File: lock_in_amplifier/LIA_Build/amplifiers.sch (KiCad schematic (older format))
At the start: 16 parts, among them U10 OP1177, U9 OP1177

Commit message: power supply, amp chain first pass
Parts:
- removed C25: 0.1u, symbol C
- removed U10: OP1177, Housings_SSOP:MSOP-8-1EP_3x3mm_Pitch0.65mm, symbol OP1177
- added C30: 0.1u, Capacitors_SMD:C_0805, symbol C
- added J25: GAIN SEL - MID, symbol Conn_01x03
- added J28: ORDER OF MAGNITUDE SELECT, symbol Conn_01x05
- added J29: DECIMAL MULTIPLIER SELECT, symbol Conn_01x04
- added R16, R37, R40: 100k, Resistors_SMD:R_0805, symbol R
- added R17, R38, R39, R41: 10k, Resistors_SMD:R_0805, symbol R
- added R18, R42: 1k, Resistors_SMD:R_0805, symbol R
- added R19, R20: 1M, Resistors_SMD:R_0805, symbol R
- added U1: LM358, symbol LM358
- added U12: NC7SB3157, symbol NC7SB3157
- C23, C24, C26: footprint (none) -> Capacitors_SMD:C_0805
- R22, R23, R24, R26, R27, R28, R29, R30, R31: footprint (none) -> Resistors_SMD:R_0805
- R25: value 10k -> 100k; footprint (none) -> Resistors_SMD:R_0805
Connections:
- wire segments 40 -> 86
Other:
- note added: "1x2x5x select\n5x\n2x\n1x"
- note added: "GAIN SELECTION BLOCK. COMP. CT. MIN. W/ PARALLEL AND SERRIES COMPONENTS.\nALL GAINS V/V\n1000X\n500X\n200X\n100X\n50X\n20X\n10X\n5X\n2X\n1X"
- note added: "SP3T"
- note added: "SP4T"
- note added: "SPDT SWITCH\n"
- note added: "lower resistance values - higher current less resistor noise?"
- note added: "order of magnitude selector\n1000x\n100x\n10x\n1x"
- note added: "reason not to do this noise wise? issues with resistor noise?\nreplace last amp with lm358 or similar?"
- note removed: "dip switches\n"
- note removed: "reason not to do this noise wise? issues with resistor noise?"
- moved on the sheet: C23, C24, C26, R22, R23, R26, R27, R28, R29, R30, R31, U9

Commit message: initial transimpedance selection, lna refinement
amp overload led
switch comps added
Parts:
- removed J25: GAIN SEL - MID, symbol Conn_01x03
- removed J28: ORDER OF MAGNITUDE SELECT, symbol Conn_01x05
- removed J29: DECIMAL MULTIPLIER SELECT, symbol Conn_01x04
- removed U12: NC7SB3157, symbol NC7SB3157
- added C22: 0.1u, Capacitors_SMD:C_0805, symbol C
- added R53: 100k, symbol R
- added R54: 100, symbol R
- added S2: MID AMP GAIN SEL, symbol SPDT
- added S3: REF V SEL, symbol SPDT
- added S7: MAG SEL, symbol SP4T
- added S8: DECIMAL MULT SEL, symbol SP3T
- U1: footprint (none) -> SMD_Packages:SOIC-8-N
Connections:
- wire segments 86 -> 93
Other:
- note added: "reason not to do this noise wise? issues with resistor noise?"
- note removed: "SP3T"
- note removed: "SP4T"
- note removed: "reason not to do this noise wise? issues with resistor noise?\nreplace last amp with lm358 or similar?"
- moved on the sheet: C23, C24, C26, C30, R16, R17, R18, R19, R20, R22, R23, R24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

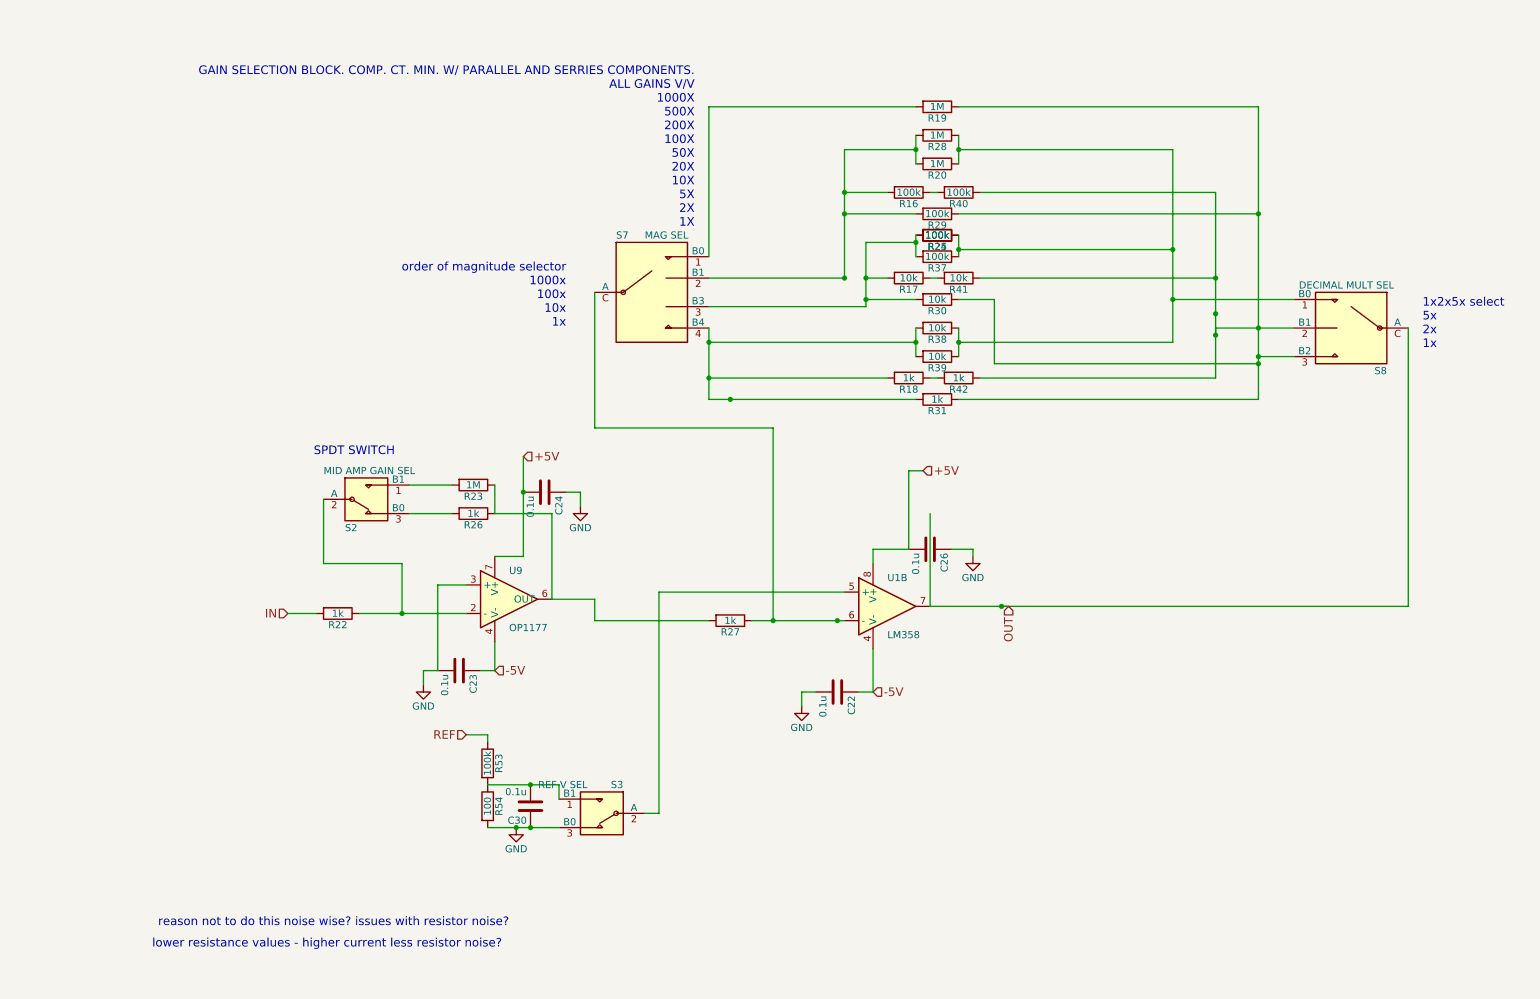
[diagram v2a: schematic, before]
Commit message: switch footprints, lm833 usage, pll investigation
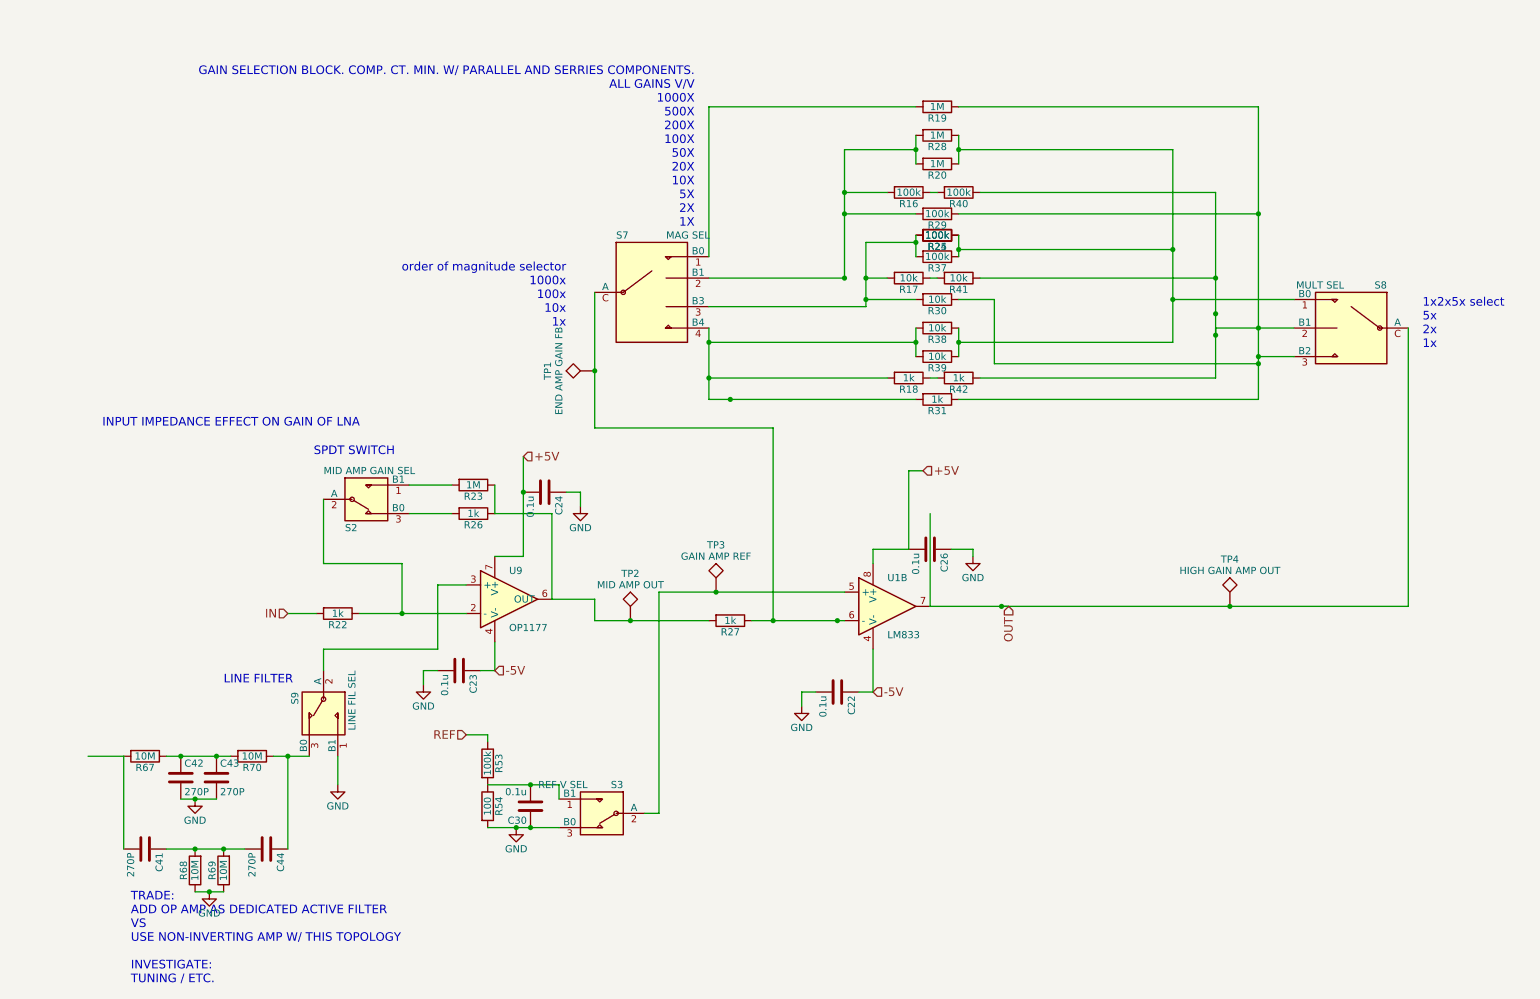
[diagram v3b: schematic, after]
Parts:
- added C41, C42, C43, C44: 270P, symbol C
- added R67, R68, R69, R70: 10M, symbol R
- added S9: LINE FIL SEL, footprints:SPDT_OS102011MS2QN1, symbol SPDT
- added TP1: END AMP GAIN FB, symbol TEST
- added TP2: MID AMP OUT, symbol TEST
- added TP3: GAIN AMP REF, symbol TEST
- added TP4: HIGH GAIN AMP OUT, symbol TEST
- S2, S3: footprint (none) -> footprints:SPDT_OS102011MS2QN1
- S7: footprint (none) -> footprints:SP4T_C&K_SS-14D0839-VG
- S8: value DECIMAL MULT SEL -> MULT SEL; footprint (none) -> footprints:SP3T_CK_SS-14D0839-VG
- U1: value LM358 -> LM833
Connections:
- net GND: now also C42.2, C43.2, R68.1, R69.1, S9.1 (B1); no longer U9.3 (+)
- net OUT: now also TP4.1
- net at S3.2 (A), U1.5 (+): now also TP3.1
- net at R27.1, S7.C (A), U1.6 (-): now also TP1.1
- net at R23.1, R26.1, R27.2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: now also TP2.1
- new net: S9.2 (A), U9.3 (+)
- new net: C44.1, R70.1, S9.3 (B0)
- new net: C42.1, C43.1, R67.1, R70.2
- new net: C41.2, R67.2
- new net: C41.1, C44.2, R68.2, R69.2
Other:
- note added: "INPUT IMPEDANCE EFFECT ON GAIN OF LNA"
- note added: "LINE FILTER"
- note added: "TRADE:\nADD OP AMP AS DEDICATED ACTIVE FILTER\nVS\nUSE NON-INVERTING AMP W/ THIS TOPOLOGY\n\nINVESTIGATE:\nTUNING / ETC."
- note removed: "lower resistance values - higher current less resistor noise?"
- note removed: "reason not to do this noise wise? issues with resistor noise?"

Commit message: PLL initial implementation
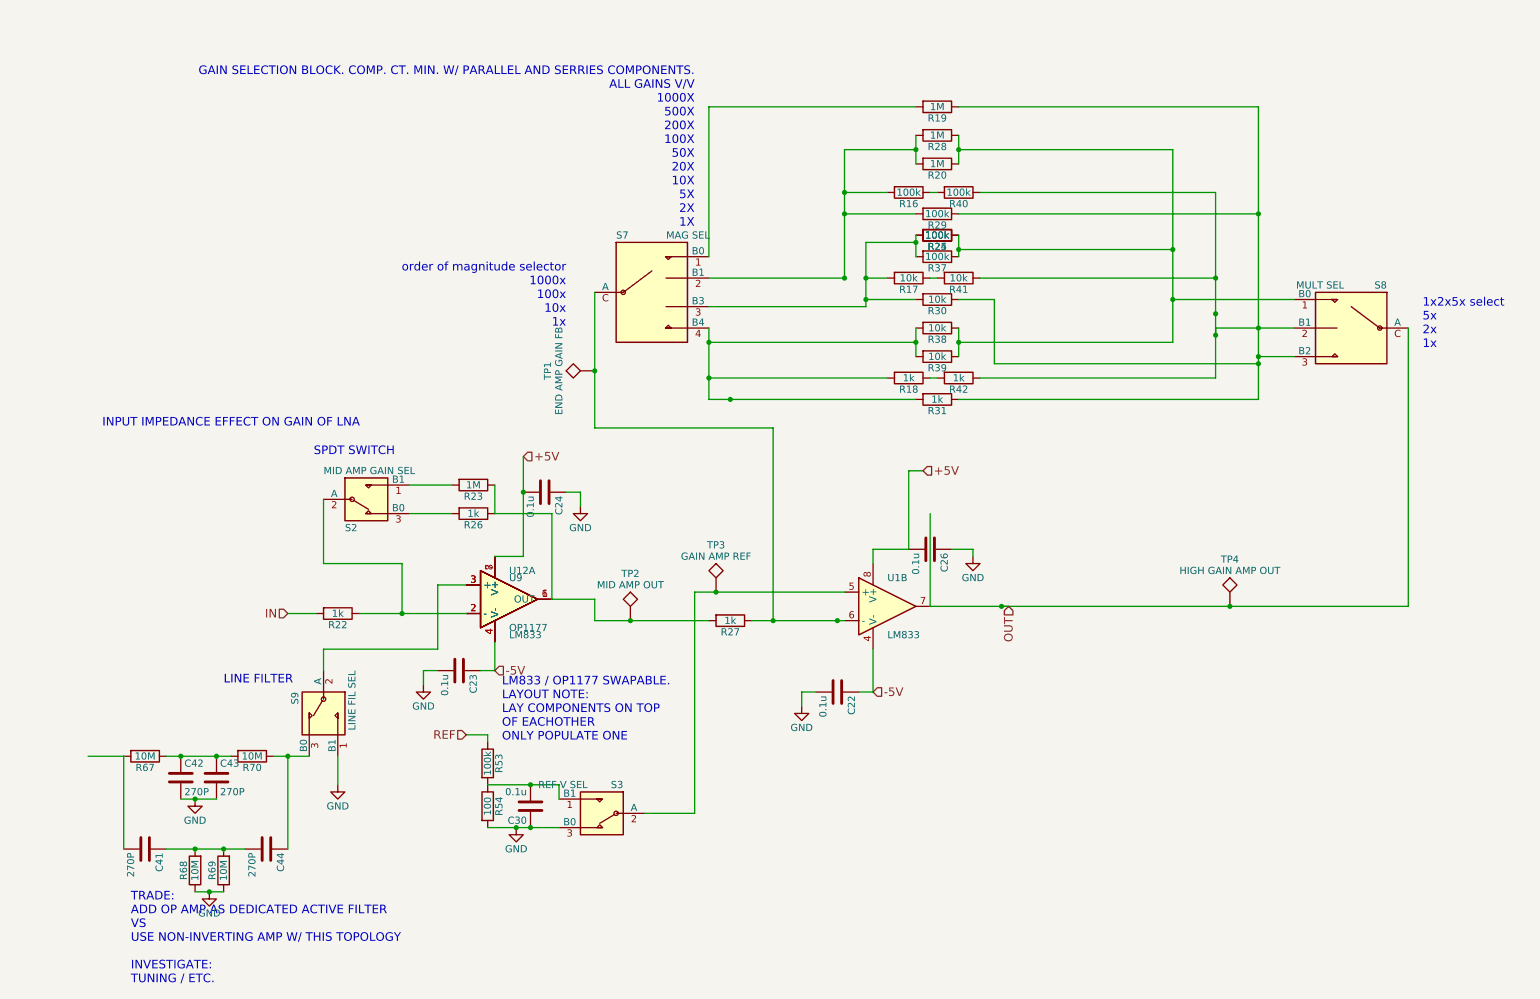
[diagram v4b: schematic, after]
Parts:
- added U12: LM833, symbol LM833
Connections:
- net +5V: now also U12.8 (V+)
- net -5V: now also U12.4 (V-)
- net at R22.1, S2.2 (A), U9.2 (-): now also U12.2 (-)
- net at R23.1, R26.1, R27.2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: now also U12.1
- net at S9.2 (A), U9.3 (+): now also U12.3 (+)
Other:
- note added: "LM833 / OP1177 SWAPABLE.\nLAYOUT NOTE: \nLAY COMPONENTS ON TOP \nOF EACHOTHER\nONLY POPULATE ONE"
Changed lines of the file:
@@
 $EndComp
 $Comp
-L GND #PWR055
+L GND #PWR60
 U 1 1 5A225760
 P 7050 4350
-F 0 "#PWR055" H 7050 4100 50  0001 C CNN
+F 0 "#PWR60" H 7050 4100 50  0001 C CNN
 F 1 "GND" H 7050 4200 50  0000 C CNN
 F 2 "" H 7050 4350 50  0001 C CNN
@@
 $EndComp
 $Comp
-L GND #PWR056
+L GND #PWR56
 U 1 1 5A2257E8
 P 3200 5250
-F 0 "#PWR056" H 3200 5000 50  0001 C CNN
+F 0 "#PWR56" H 3200 5000 50  0001 C CNN
 F 1 "GND" H 3200 5100 50  0000 C CNN
 F 2 "" H 3200 5250 50  0001 C CNN
@@
 $EndComp
 $Comp
-L GND #PWR057
+L GND #PWR58
 U 1 1 5A22582C
 P 4300 4000
-F 0 "#PWR057" H 4300 3750 50  0001 C CNN
+F 0 "#PWR58" H 4300 3750 50  0001 C CNN
 F 1 "GND" H 4300 3850 50  0000 C CNN
 F 2 "" H 4300 4000 50  0001 C CNN
@@
 U 1 1 5A22674B
 P 3800 4650
-F 0 "U9" H 3800 4850 50  0000 L CNN
+F 0 "U9" H 3800 4800 50  0000 L CNN
 F 1 "OP1177" H 3800 4450 50  0000 L CNN
 F 2 "Housings_SSOP:MSOP-8-1EP_3x3mm_Pitch0.65mm" H 4050 4350 50  0001 C CNN
@@
 $EndComp
 $Comp
-L GND #PWR058
+L GND #PWR57
 U 1 1 5A237D65
 P 3850 6250
-F 0 "#PWR058" H 3850 6000 50  0001 C CNN
+F 0 "#PWR57" H 3850 6000 50  0001 C CNN
 F 1 "GND" H 3850 6100 50  0000 C CNN
 F 2 "" H 3850 6250 50  0001 C CNN
@@
 	3900 4350 3700 4350
 Wire Wire Line
-	3900 3650 3900 4350
-Wire Wire Line
-	6750 4700 7300 4700
+	3900 3650 3900 3900
+Wire Wire Line
+	3900 3900 3900 4350
+Wire Wire Line
+	6750 4700 7250 4700
+Wire Wire Line
+	7250 4700 7300 4700
 Wire Wire Line
 	6750 4050 6750 4700
@@
 	3200 5150 3200 5250
 Wire Wire Line
-	5500 4800 6150 4800
+	5500 4800 5650 4800
+Wire Wire Line
+	5650 4800 6100 4800
+Wire Wire Line
+	6100 4800 6150 4800
 Connection ~ 6100 4800
 Wire Wire Line
@@
 	4100 4650 4400 4650
 Wire Wire Line
-	4750 6150 4850 6150
-Wire Wire Line
-	3650 6250 4150 6250
+	4750 6150 5100 6150
+Wire Wire Line
+	3650 6250 3850 6250
+Wire Wire Line
+	3850 6250 3950 6250
+Wire Wire Line
+	3950 6250 4150 6250
 Connection ~ 3950 6250
 Wire Wire Line
-	3650 5950 4150 5950
+	3650 5950 3950 5950
+Wire Wire Line
+	3950 5950 4150 5950
 Wire Wire Line
 	4150 5950 4150 6050
@@
 	4400 4650 4400 4800
 Wire Wire Line
-	4400 4800 5200 4800
-Wire Wire Line
-	4850 6150 4850 4600
-Wire Wire Line
-	4850 4600 6150 4600
+	4400 4800 4650 4800
+Wire Wire Line
+	4650 4800 5200 4800
+Wire Wire Line
+	5100 6150 5100 4600
+Wire Wire Line
+	5100 4600 5250 4600
+Wire Wire Line
+	5250 4600 6150 4600
 Wire Wire Line
 	3700 3850 3700 4050
@@
 	3400 4050 3100 4050
 Wire Wire Line
-	2750 4750 3500 4750
-Wire Wire Line
-	6950 2750 6950 2950
-Wire Wire Line
-	6950 2100 6950 2250
-Wire Wire Line
-	6950 1400 6950 1600
+	2750 4750 3050 4750
+Wire Wire Line
+	3050 4750 3500 4750
+Wire Wire Line
+	6950 2750 6950 2850
+Wire Wire Line
+	6950 2850 6950 2950
+Wire Wire Line
+	6950 2100 6950 2200
+Wire Wire Line
+	6950 2200 6950 2250
+Wire Wire Line
+	6950 1400 6950 1500
+Wire Wire Line
+	6950 1500 6950 1600
 Connection ~ 6950 1500
 Connection ~ 6950 2200
@@
 	6800 1800 6750 1800
 Wire Wire Line
-	6650 1400 6650 1600
-Wire Wire Line
-	6650 2100 6650 2250
-Wire Wire Line
-	6650 2750 6650 2950
+	6650 1400 6650 1500
+Wire Wire Line
+	6650 1500 6650 1600
+Wire Wire Line
+	6650 2100 6650 2150
+Wire Wire Line
+	6650 2150 6650 2250
+Wire Wire Line
+	6650 2750 6650 2850
+Wire Wire Line
+	6650 2850 6650 2950
 Connection ~ 6650 1500
 Connection ~ 6650 2850
@@
 Connection ~ 7250 4700
 Wire Wire Line
-	7250 4700 10100 4700
+	7250 4700 8850 4700
+Wire Wire Line
+	8850 4700 10100 4700
 Text Notes 10200 2900 0    60   ~ 0
 1x2x5x select\n5x\n2x\n1x
 Wire Wire Line
-	9050 1200 9050 3250
+	9050 1200 9050 1950
+Wire Wire Line
+	9050 1950 9050 2750
+Wire Wire Line
+	9050 2750 9050 2950
+Wire Wire Line
+	9050 2950 9050 3000
+Wire Wire Line
+	9050 3000 9050 3250
 Wire Wire Line
 	9050 3250 6950 3250
@@
 Connection ~ 9050 1950
 Wire Wire Line
-	8750 1800 8750 3100
+	8750 1800 8750 2400
+Wire Wire Line
+	8750 2400 8750 2650
+Wire Wire Line
+	8750 2650 8750 2800
+Wire Wire Line
+	8750 2800 8750 3100
 Wire Wire Line
 	8750 1800 7100 1800
@@
 Connection ~ 9050 3000
 Wire Wire Line
-	8450 1500 8450 2850
+	8450 1500 8450 2200
+Wire Wire Line
+	8450 2200 8450 2550
+Wire Wire Line
+	8450 2550 8450 2850
 Wire Wire Line
 	8450 2850 6950 2850
@@
 	5200 1200 6650 1200
 Wire Wire Line
-	5200 3250 6650 3250
+	5200 3250 5350 3250
+Wire Wire Line
+	5350 3250 6650 3250
 Wire Wire Line
 	6300 2550 6650 2550
@@
 	6450 2400 6300 2400
 Wire Wire Line
-	6300 2150 6300 2600
+	6300 2150 6300 2400
+Wire Wire Line
+	6300 2400 6300 2550
+Wire Wire Line
+	6300 2550 6300 2600
 Connection ~ 6300 2550
 Wire Wire Line
@@
 	6150 1950 6650 1950
 Wire Wire Line
-	6150 1500 6150 2400
+	6150 1500 6150 1800
+Wire Wire Line
+	6150 1800 6150 1950
+Wire Wire Line
+	6150 1950 6150 2400
 Wire Wire Line
 	6450 1800 6150 1800
@@
 $EndComp
 $Comp
-L GND #PWR059
+L GND #PWR59
 U 1 1 5A275732
 P 5850 5400
-F 0 "#PWR059" H 5850 5150 50  0001 C CNN
+F 0 "#PWR59" H 5850 5150 50  0001 C CNN
 F 1 "GND" H 5850 5250 50  0000 C CNN
 F 2 "" H 5850 5400 50  0001 C CNN
@@
 Connection ~ 9050 2950
 Wire Wire Line
-	8750 2750 9300 2750
+	8750 2750 9050 2750
+Wire Wire Line
+	9050 2750 9300 2750
 Wire Wire Line
 	8750 2750 8750 2800
@@
 	5200 1200 5200 2250
 Wire Wire Line
-	5200 2750 5200 3250
+	5200 2750 5200 2850
+Wire Wire Line
+	5200 2850 5200 3100
+Wire Wire Line
+	5200 3100 5200 3250
 Connection ~ 5350 3250
 Wire Wire Line
@@
 Connection ~ 6150 2400
 Wire Wire Line
-	4400 2500 4400 3450
+	4400 2500 4400 3050
+Wire Wire Line
+	4400 3050 4400 3450
 Wire Wire Line
 	4400 3450 5650 3450
@@
 	2500 5000 2500 5150
 $Comp
-L GND #PWR060
+L GND #PWR55
 U 1 1 5A257877
 P 2600 5950
-F 0 "#PWR060" H 2600 5700 50  0001 C CNN
+F 0 "#PWR55" H 2600 5700 50  0001 C CNN
 F 1 "GND" H 2600 5800 50  0000 C CNN
 F 2 "" H 2600 5950 50  0001 C CNN
@@
 $EndComp
 $Comp
-L GND #PWR061
+L GND #PWR53
 U 1 1 5A259E13
 P 1600 6050
-F 0 "#PWR061" H 1600 5800 50  0001 C CNN
+F 0 "#PWR53" H 1600 5800 50  0001 C CNN
 F 1 "GND" H 1600 5900 50  0000 C CNN
 F 2 "" H 1600 6050 50  0001 C CNN
@@
 $EndComp
 Wire Wire Line
-	1500 6050 1750 6050
+	1500 6050 1600 6050
+Wire Wire Line
+	1600 6050 1750 6050
 Connection ~ 1600 6050
 Wire Wire Line
-	1400 5750 1850 5750
+	1400 5750 1500 5750
+Wire Wire Line
+	1500 5750 1750 5750
+Wire Wire Line
+	1750 5750 1850 5750
 Connection ~ 1500 5750
 Connection ~ 1750 5750
 Wire Wire Line
-	2150 5750 2400 5750
+	2150 5750 2250 5750
+Wire Wire Line
+	2250 5750 2400 5750
 Wire Wire Line
 	2250 5750 2250 6400
 Wire Wire Line
-	1400 6400 1950 6400
+	1400 6400 1600 6400
+Wire Wire Line
+	1600 6400 1800 6400
+Wire Wire Line
+	1800 6400 1950 6400
 Connection ~ 1800 6400
 Connection ~ 1600 6400
@@
 	1100 5750 850  5750
 $Comp
-L GND #PWR062
+L GND #PWR54
 U 1 1 5A25B123
 P 1700 6700
-F 0 "#PWR062" H 1700 6450 50  0001 C CNN
+F 0 "#PWR54" H 1700 6450 50  0001 C CNN
 F 1 "GND" H 1700 6550 50  0000 C CNN
 F 2 "" H 1700 6700 50  0001 C CNN
@@
 $EndComp
 Wire Wire Line
-	1600 6700 1800 6700
+	1600 6700 1700 6700
+Wire Wire Line
+	1700 6700 1800 6700
 Connection ~ 1700 6700
 Text Notes 950  3450 0    60   ~ 0
@@
 Text Notes 1150 7350 0    60   ~ 0
 TRADE:\nADD OP AMP AS DEDICATED ACTIVE FILTER\nVS\nUSE NON-INVERTING AMP W/ THIS TOPOLOGY\n\nINVESTIGATE:\nTUNING / ETC.
+$Comp
+L LM833 U12
+U 1 1 5A26D5E1
+P 3800 4650
+F 0 "U12" H 3800 4850 50  0000 L CNN
+F 1 "LM833" H 3800 4400 50  0000 L CNN
+F 2 "" H 3800 4650 50  0001 C CNN
+F 3 "" H 3800 4650 50  0001 C CNN
+	1    3800 4650
+	1    0    0    -1
+$EndComp
+Text Notes 3750 5650 0    60   ~ 0
+LM833 / OP1177 SWAPABLE.\nLAYOUT NOTE: \nLAY COMPONENTS ON TOP \nOF EACHOTHER\nONLY POPULATE ONE
 $EndSCHEMATC
